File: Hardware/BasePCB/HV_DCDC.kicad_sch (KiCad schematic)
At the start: 12 parts, among them U2 DCDC

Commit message: 0 unrouted nets :0 (all my footprints are mad at me)
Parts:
- TP23: footprint UTSVT_Special:TestPoint_HEX_3mmID -> TestPoint:TestPoint_THTPad_D3.0mm_Drill1.5mm
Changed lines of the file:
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@@
 			)
 		)
-		(property "Footprint" "UTSVT_Special:TestPoint_HEX_3mmID"
+		(property "Footprint" "TestPoint:TestPoint_THTPad_D3.0mm_Drill1.5mm"
 			(at 105.41 111.76 0)
 			(effects

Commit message: BOM
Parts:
- TP13, TP15, TP17, TP22, TP23, TP4, TP5, TP6: now left out of the parts list
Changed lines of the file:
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@@
 		(unit 1)
 		(exclude_from_sim no)
-		(in_bom yes)
+		(in_bom no)
 		(on_board yes)
 		(dnp no)
@@
 		(unit 1)
 		(exclude_from_sim no)
-		(in_bom yes)
+		(in_bom no)
 		(on_board yes)
 		(dnp no)
@@
 		(unit 1)
 		(exclude_from_sim no)
-		(in_bom yes)
+		(in_bom no)
 		(on_board yes)
 		(dnp no)
@@
 		(unit 1)
 		(exclude_from_sim no)
-		(in_bom yes)
+		(in_bom no)
 		(on_board yes)
 		(dnp no)
@@
 		(unit 1)
 		(exclude_from_sim no)
-		(in_bom yes)
+		(in_bom no)
 		(on_board yes)
 		(dnp no)
@@
 		(unit 1)
 		(exclude_from_sim no)
-		(in_bom yes)
+		(in_bom no)
 		(on_board yes)
 		(dnp no)
@@
 		(unit 1)
 		(exclude_from_sim no)
-		(in_bom yes)
+		(in_bom no)
 		(on_board yes)
 		(dnp no)
@@
 		(unit 1)
 		(exclude_from_sim no)
-		(in_bom yes)
-		(on_board yes)
-		(dnp no)
+		(in_bom no)
+		(on_board yes)
+		(dnp no)

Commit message: bom 2
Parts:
- F2: P/N (none) -> 05200101Z
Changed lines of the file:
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@@
+			)
+		)
+		(property "P/N" "05200101Z"
+			(at 88.9 67.31 0)
+			(effects
+				(font
+					(size 1.27 1.27)
+				)
 			)
 		)

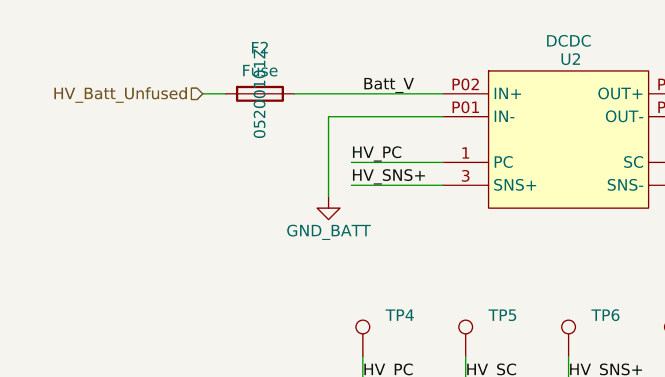
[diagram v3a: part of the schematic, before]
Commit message: add hall effect sensor
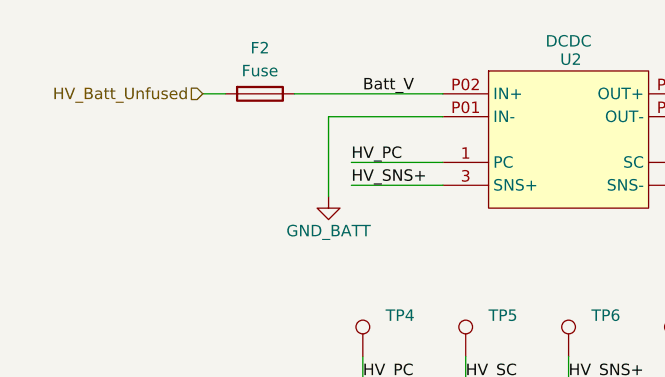
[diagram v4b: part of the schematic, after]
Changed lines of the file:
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@@
 			)
 		)
-		(property "Datasheet" "https://www.lcsc.com/datasheet/C7371904.pdf"
+		(property "Datasheet" "~"
 			(at 152.4 107.95 0)
 			(effects
@@
 			)
 		)
-		(property "Description" ""
+		(property "Description" "Fuse"
 			(at 88.9 67.31 0)
 			(effects
@@
 					(size 1.27 1.27)
 				)
+				(hide yes)
 			)
 		)
@@
 					(size 1.27 1.27)
 				)
-			)
-		)
+				(hide yes)
+			)
+		)

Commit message: add JLC p/n
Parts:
- D19: Assemble (none) -> Y; LSCC P/N (none) -> C7371904
- F2, TP13, TP15, TP17, TP22, TP23, TP4, TP5, TP6: Assemble (none) -> N
- R31: Assemble (none) -> Y; LSCC P/N (none) -> C23162
- U2: Assemble (none) -> N; Datasheet2 https://www.vicorpower.com/documents/datasheets/ds_110vin-m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 -> (none)
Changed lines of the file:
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@@
+			)
+		)
+		(property "LSCC P/N" ""
+			(at 149.86 64.77 0)
+			(effects
+				(font
+					(size 1.27 1.27)
+				)
+				(hide yes)
+			)
+		)
+		(property "Assemble" "N"
+			(at 149.86 64.77 0)
+			(effects
+				(font
+					(size 1.27 1.27)
+				)
+				(hide yes)
 			)
 		)
@@
 			)
 		)
-		(property "Datasheet2" "https://www.vicorpower.com/documents/datasheets/ds_110vin-maxi-family.pdf"
+		(property "LSCC P/N" ""
+			(at 123.19 62.23 0)
+			(effects
+				(font
+					(size 1.27 1.27)
+				)
+				(hide yes)
+			)
+		)
+		(property "Assemble" "N"
 			(at 123.19 62.23 0)
 			(effects
@@
 			)
 		)
+		(property "LSCC P/N" ""
+			(at 100.33 111.76 0)
+			(effects
+				(font
+					(size 1.27 1.27)
+				)
+				(hide yes)
+			)
+		)
+		(property "Assemble" "N"
+			(at 100.33 111.76 0)
+			(effects
+				(font
+					(size 1.27 1.27)
+				)
+				(hide yes)
+			)
+		)
 		(pin "1"
 		)
@@
 			)
 		)
+		(property "LSCC P/N" ""
+			(at 111.76 96.52 0)
+			(effects
+				(font
+					(size 1.27 1.27)
+				)
+				(hide yes)
+			)
+		)
+		(property "Assemble" "N"
+			(at 111.76 96.52 0)
+			(effects
+				(font
+					(size 1.27 1.27)
+				)
+				(hide yes)
+			)
+		)
 		(pin "1"
 		)
@@
 		)
 		(property "P/N" "CRCW06034K30FKTA "
+			(at 152.4 97.79 0)
+			(effects
+				(font
+					(size 1.27 1.27)
+				)
+				(hide yes)
+			)
+		)
+		(property "LSCC P/N" "C23162"
+			(at 152.4 97.79 0)
+			(effects
+				(font
+					(size 1.27 1.27)
+				)
+				(hide yes)
+			)
+		)
+		(property "Assemble" "Y"
 			(at 152.4 97.79 0)
 			(effects
@@
 			)
 		)
+		(property "LSCC P/N" ""
+			(at 134.62 96.52 0)
+			(effects
+				(font
+					(size 1.27 1.27)
+				)
+				(hide yes)
+			)
+		)
+		(property "Assemble" "N"
+			(at 134.62 96.52 0)
+			(effects
+				(font
+					(size 1.27 1.27)
+				)
+				(hide yes)
+			)
+		)
 		(pin "1"
 		)
@@
 			)
 		)
+		(property "LSCC P/N" "C7371904"
+			(at 152.4 107.95 90)
+			(effects
+				(font
+					(size 1.27 1.27)
+				)
+				(hide yes)
+			)
+		)
+		(property "Assemble" "Y"
+			(at 152.4 107.95 90)
+			(effects
+				(font
+					(size 1.27 1.27)
+				)
+				(hide yes)
+			)
+		)
 		(pin "2"
 		)
@@
 			)
 		)
+		(property "LSCC P/N" ""
+			(at 135.89 111.76 0)
+			(effects
+				(font
+					(size 1.27 1.27)
+				)
+				(hide yes)
+			)
+		)
+		(property "Assemble" "N"
+			(at 135.89 111.76 0)
+			(effects
+				(font
+					(size 1.27 1.27)
+				)
+				(hide yes)
+			)
+		)
 		(pin "1"
 		)
@@
 			)
 		)
+		(property "LSCC P/N" ""
+			(at 100.33 96.52 0)
+			(effects
+				(font
+					(size 1.27 1.27)
+				)
+				(hide yes)
+			)
+		)
+		(property "Assemble" "N"
+			(at 100.33 96.52 0)
+			(effects
+				(font
+					(size 1.27 1.27)
+				)
+				(hide yes)
+			)
+		)
 		(pin "1"
 		)
@@
 			)
 		)
+		(property "LSCC P/N" ""
+			(at 123.19 111.76 0)
+			(effects
+				(font
+					(size 1.27 1.27)
+				)
+				(hide yes)
+			)
+		)
+		(property "Assemble" "N"
+			(at 123.19 111.76 0)
+			(effects
+				(font
+					(size 1.27 1.27)
+				)
+				(hide yes)
+			)
+		)
 		(pin "1"
 		)
@@
 			)
 		)
+		(property "LSCC P/N" ""
+			(at 88.9 67.31 90)
+			(effects
+				(font
+					(size 1.27 1.27)
+				)
+				(hide yes)
+			)
+		)
+		(property "Assemble" "N"
+			(at 88.9 67.31 90)
+			(effects
+				(font
+					(size 1.27 1.27)
+				)
+				(hide yes)
+			)
+		)
 		(pin "2"
 		)
@@
 			(at 123.19 96.52 0)
 			(effects
+				(font
+					(size 1.27 1.27)
+				)
+				(hide yes)
+			)
+		)
+		(property "LSCC P/N" ""
+			(at 123.19 96.52 0)
+			(effects
+				(font
+					(size 1.27 1.27)
+				)
+				(hide yes)
+			)
+		)
+		(property "Assemble" "N"
+			(at 123.19 96.52 0)
+			(effects

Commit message: lil shah part 1
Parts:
- removed F2: Fuse, LV Carrier Library:FUSE_05200101Z_LTF, symbol Device:Fuse
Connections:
- net Batt_V is gone; now on net HV_Batt_Unfused: TP17.1, U2.P02 (IN+)
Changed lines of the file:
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@@
 	(wire
 		(pts
-			(xy 82.55 67.31) (xy 85.09 67.31)
+			(xy 82.55 67.31) (xy 109.22 67.31)
 		)
 		(stroke
@@
 		(pts
 			(xy 100.33 96.52) (xy 100.33 99.06)
-		)
-		(stroke
-			(width 0)
-			(type default)
-		)
-	)
-	(wire
-		(pts
-			(xy 92.71 67.31) (xy 109.22 67.31)
 		)
 		(stroke
@@
 					(unit 1)
 				)
-			)
-		)
-	)
-	(symbol
-		(lib_id "Device:Fuse")
-		(at 88.9 67.31 270)
-		(unit 1)
-		(exclude_from_sim no)
-		(in_bom yes)
-		(on_board yes)
-		(dnp no)
-		(fields_autoplaced yes)
-		(property "Reference" "F2"
-			(at 88.9 62.23 90)
-			(effects
-				(font
-					(size 1.27 1.27)
-				)
-			)
-		)
-		(property "Value" "Fuse"
-			(at 88.9 64.77 90)
-			(effects
-				(font
-					(size 1.27 1.27)
-				)
-			)
-		)
-		(property "Footprint" "LV Carrier Library:FUSE_05200101Z_LTF"
-			(at 88.9 65.532 90)
-			(effects
-				(font
-					(size 1.27 1.27)
-				)
-				(hide yes)
-			)
-		)
-		(property "Datasheet" "~"
-			(at 88.9 67.31 0)
-			(effects
-				(font
-					(size 1.27 1.27)
-				)
-				(hide yes)
-			)
-		)
-		(property "Description" "Fuse"
-			(at 88.9 67.31 0)
-			(effects
-				(font
-					(size 1.27 1.27)
-				)
-				(hide yes)
-			)
-		)
-		(property "P/N" "05200101Z"
-			(at 88.9 67.31 0)
-			(effects
-				(font
-					(size 1.27 1.27)
-				)
-				(hide yes)
-			)
-		)
-		(property "LSCC P/N" ""
-			(at 88.9 67.31 90)
-			(effects
-				(font
-					(size 1.27 1.27)
-				)
-				(hide yes)
-			)
-		)
-		(property "Assemble" "N"
-			(at 88.9 67.31 90)
-			(effects
-				(font
-					(size 1.27 1.27)
-				)
-				(hide yes)
-			)
-		)
-		(pin "2"
-		)
-		(pin "1"
-		)
-		(instances
-			(project "LV Carrier Board"
-				(path "/c5c5922b-1600-4b67-acf3-33264cecd75b/eb5e61c4-fcb9-4f3b-9225-002a6ddfe10f"
-					(reference "F2")
-					(unit 1)
-				)

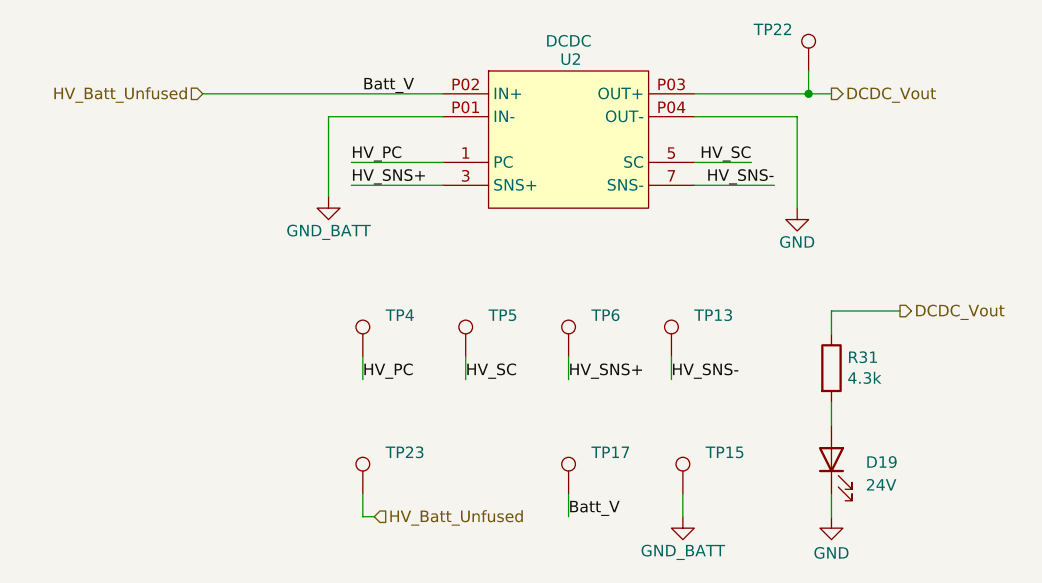
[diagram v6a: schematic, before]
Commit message: new hall effect IC
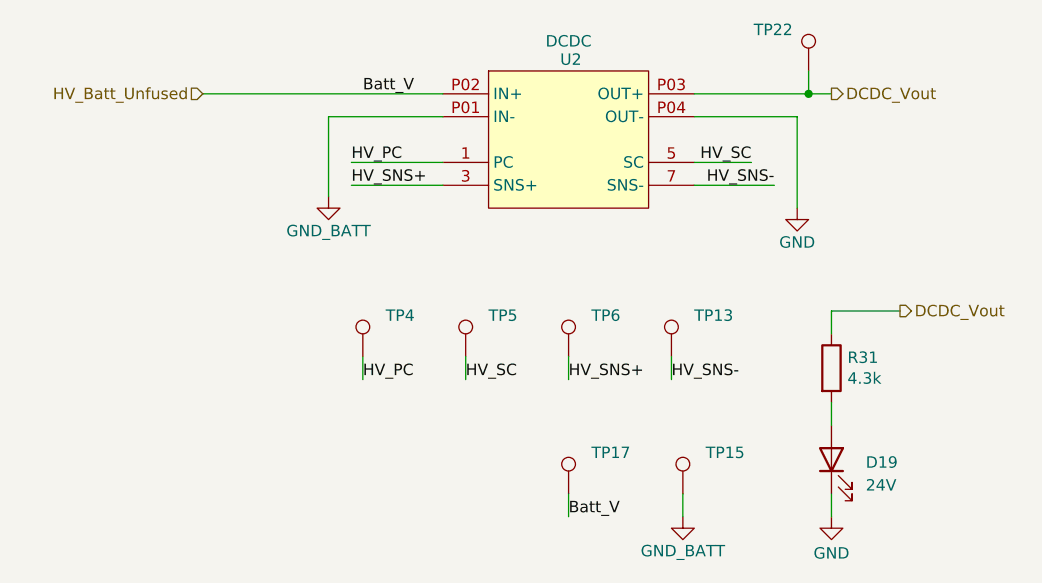
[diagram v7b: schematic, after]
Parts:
- removed TP23: TestPoint, TestPoint:TestPoint_THTPad_D3.0mm_Drill1.5mm, symbol Connector:TestPoint
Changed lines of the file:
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@@
-	(wire
-		(pts
-			(xy 100.33 111.76) (xy 100.33 114.3)
-		)
-		(stroke
-			(width 0)
-			(type default)
-		)
-	)
 	(wire
 		(pts
@@
 		(pts
 			(xy 152.4 91.44) (xy 160.02 91.44)
-		)
-		(stroke
-			(width 0)
-			(type default)
-		)
-	)
-	(wire
-		(pts
-			(xy 100.33 114.3) (xy 101.6 114.3)
 		)
 		(stroke
@@
 			)
 			(justify right)
-		)
-	)
-	(hierarchical_label "HV_Batt_Unfused"
-		(shape input)
-		(at 101.6 114.3 0)
-		(effects
-			(font
-				(size 1.27 1.27)
-			)
-			(justify left)
 		)
 	)
@@
 					(unit 1)
 				)
-			)
-		)
-	)
-	(symbol
-		(lib_id "Connector:TestPoint")
-		(at 100.33 111.76 0)
-		(unit 1)
-		(exclude_from_sim no)
-		(in_bom no)
-		(on_board yes)
-		(dnp no)
-		(fields_autoplaced yes)
-		(property "Reference" "TP23"
-			(at 102.87 107.1879 0)
-			(effects
-				(font
-					(size 1.27 1.27)
-				)
-				(justify left)
-			)
-		)
-		(property "Value" "TestPoint"
-			(at 102.87 109.7279 0)
-			(effects
-				(font
-					(size 1.27 1.27)
-				)
-				(justify left)
-				(hide yes)
-			)
-		)
-		(property "Footprint" "TestPoint:TestPoint_THTPad_D3.0mm_Drill1.5mm"
-			(at 105.41 111.76 0)
-			(effects
-				(font
-					(size 1.27 1.27)
-				)
-				(hide yes)
-			)
-		)
-		(property "Datasheet" "~"
-			(at 105.41 111.76 0)
-			(effects
-				(font
-					(size 1.27 1.27)
-				)
-				(hide yes)
-			)
-		)
-		(property "Description" "test point"
-			(at 100.33 111.76 0)
-			(effects
-				(font
-					(size 1.27 1.27)
-				)
-				(hide yes)
-			)
-		)
-		(property "LSCC P/N" ""
-			(at 100.33 111.76 0)
-			(effects
-				(font
-					(size 1.27 1.27)
-				)
-				(hide yes)
-			)
-		)
-		(property "Assemble" "N"
-			(at 100.33 111.76 0)
-			(effects
-				(font
-					(size 1.27 1.27)
-				)
-				(hide yes)
-			)
-		)
-		(pin "1"
-		)
-		(instances
-			(project "LV Carrier Board"
-				(path "/c5c5922b-1600-4b67-acf3-33264cecd75b/eb5e61c4-fcb9-4f3b-9225-002a6ddfe10f"
-					(reference "TP23")
-					(unit 1)
-				)

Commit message: lil shah pt 3
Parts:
- D19: LSCC P/N C7371904 -> (none); LSCS P/N (none) -> C7371904
- R31: LSCC P/N C23162 -> (none); LSCS P/N (none) -> C23162
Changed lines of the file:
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@@
-			)
-		)
-		(property "LSCC P/N" ""
-			(at 149.86 64.77 0)
-			(effects
-				(font
-					(size 1.27 1.27)
-				)
-				(hide yes)
 			)
 		)
@@
 			)
 		)
-		(property "LSCC P/N" ""
-			(at 123.19 62.23 0)
-			(effects
-				(font
-					(size 1.27 1.27)
-				)
-				(hide yes)
-			)
-		)
 		(property "Assemble" "N"
 			(at 123.19 62.23 0)
@@
 			)
 		)
-		(property "LSCC P/N" ""
-			(at 111.76 96.52 0)
-			(effects
-				(font
-					(size 1.27 1.27)
-				)
-				(hide yes)
-			)
-		)
 		(property "Assemble" "N"
 			(at 111.76 96.52 0)
@@
 			)
 		)
-		(property "LSCC P/N" "C23162"
+		(property "Assemble" "Y"
 			(at 152.4 97.79 0)
 			(effects
@@
 			)
 		)
-		(property "Assemble" "Y"
+		(property "LSCS P/N" "C23162"
 			(at 152.4 97.79 0)
 			(effects
@@
 			)
 		)
-		(property "LSCC P/N" ""
-			(at 134.62 96.52 0)
-			(effects
-				(font
-					(size 1.27 1.27)
-				)
-				(hide yes)
-			)
-		)
 		(property "Assemble" "N"
 			(at 134.62 96.52 0)
@@
 			)
 		)
-		(property "LSCC P/N" "C7371904"
+		(property "Assemble" "Y"
 			(at 152.4 107.95 90)
 			(effects
@@
 			)
 		)
-		(property "Assemble" "Y"
+		(property "LSCS P/N" "C7371904"
 			(at 152.4 107.95 90)
 			(effects
@@
 			)
 		)
-		(property "LSCC P/N" ""
-			(at 135.89 111.76 0)
-			(effects
-				(font
-					(size 1.27 1.27)
-				)
-				(hide yes)
-			)
-		)
 		(property "Assemble" "N"
 			(at 135.89 111.76 0)
@@
 			)
 		)
-		(property "LSCC P/N" ""
-			(at 100.33 96.52 0)
-			(effects
-				(font
-					(size 1.27 1.27)
-				)
-				(hide yes)
-			)
-		)
 		(property "Assemble" "N"
 			(at 100.33 96.52 0)
@@
 			)
 		)
-		(property "LSCC P/N" ""
-			(at 123.19 111.76 0)
-			(effects
-				(font
-					(size 1.27 1.27)
-				)
-				(hide yes)
-			)
-		)
 		(property "Assemble" "N"
 			(at 123.19 111.76 0)
@@
 			(at 123.19 96.52 0)
 			(effects
-				(font
-					(size 1.27 1.27)
-				)
-				(hide yes)
-			)
-		)
-		(property "LSCC P/N" ""
-			(at 123.19 96.52 0)
-			(effects
